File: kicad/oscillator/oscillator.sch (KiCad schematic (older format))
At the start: 19 parts

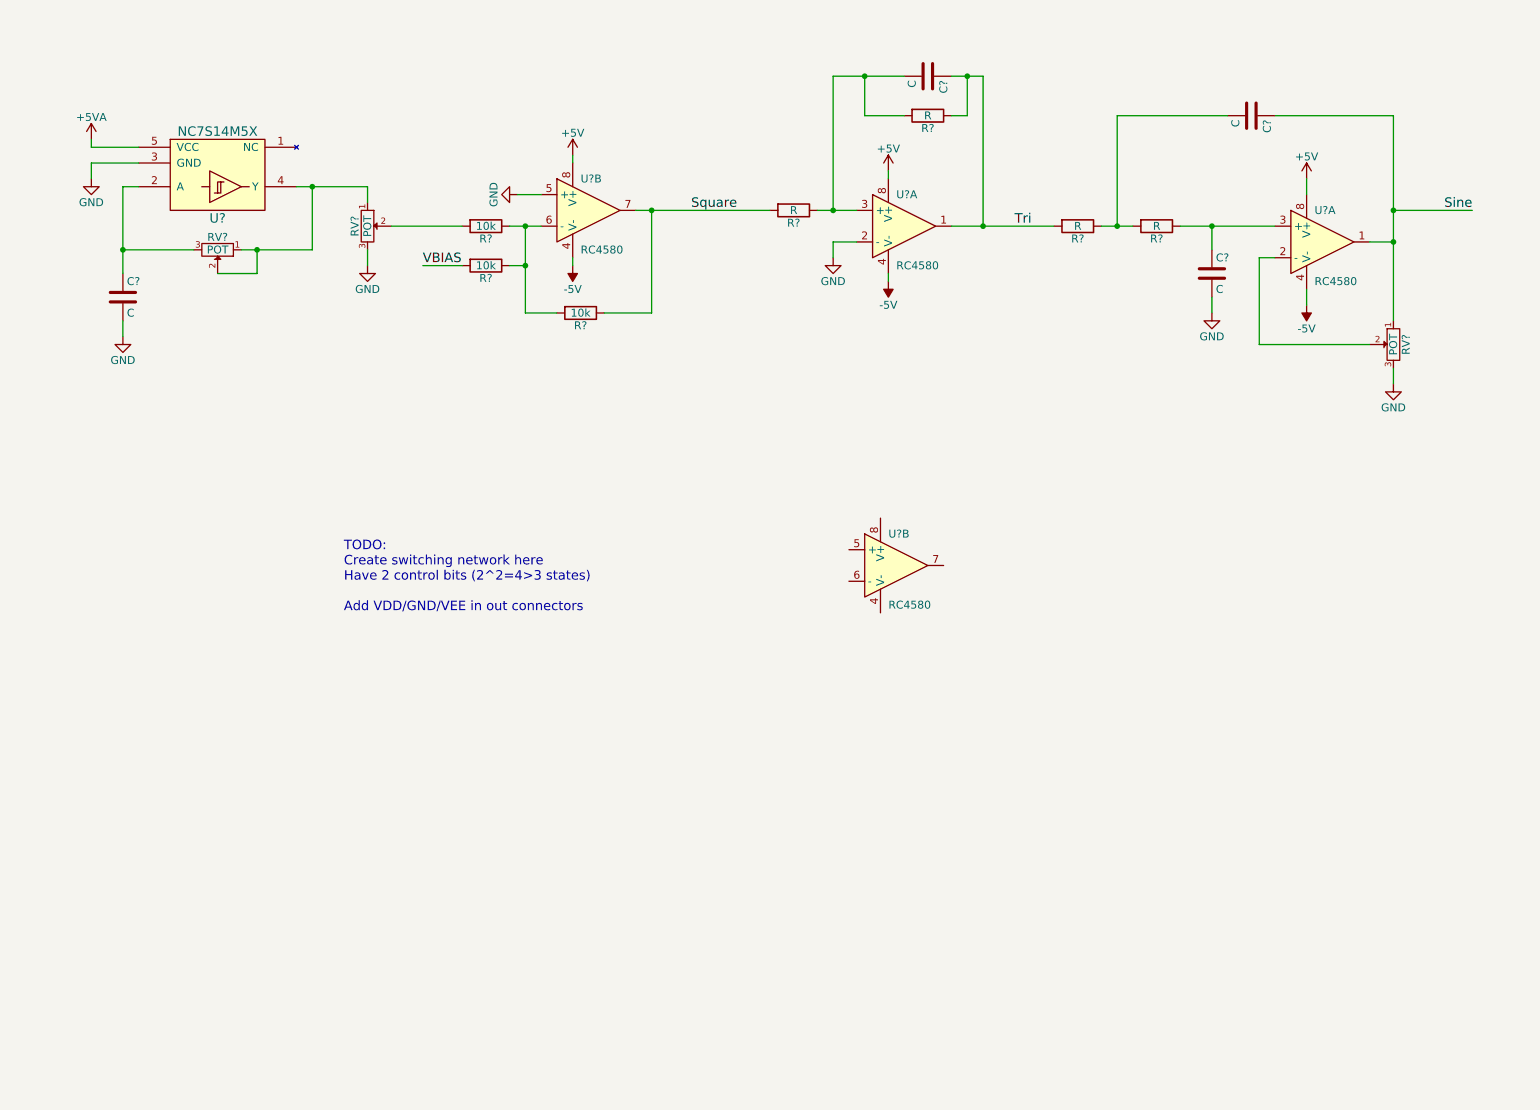
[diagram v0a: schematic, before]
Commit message: [kicad] osc schem done
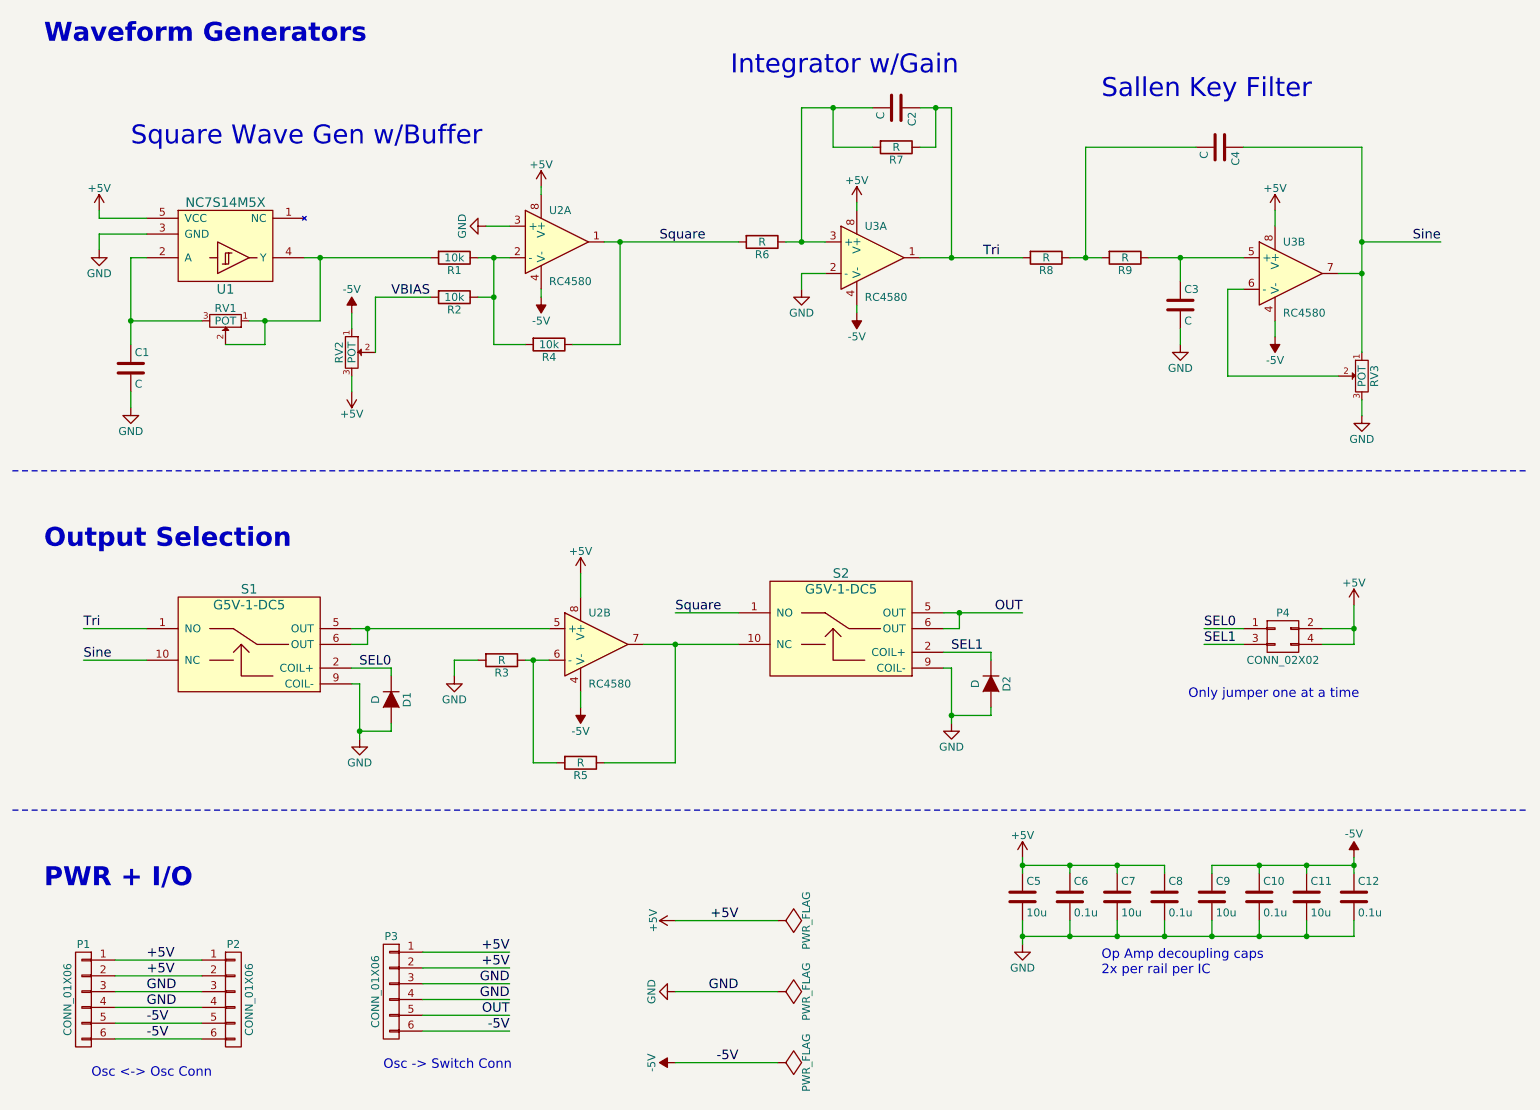
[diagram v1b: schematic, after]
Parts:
- removed RV?: POT, symbol POT
- added C10, C12, C6, C8: 0.1u, Capacitors_SMD:C_0805_HandSoldering, symbol C
- added C11, C5, C7, C9: 10u, Capacitors_SMD:C_0805_HandSoldering, symbol C
- added D1, D2: D, TO_SOT_Packages_SMD:SOT-23, symbol D
- added P1, P2, P3: CONN_01X06, Pin_Headers:Pin_Header_Angled_1x06, symbol CONN_01X06
- added P4: CONN_02X02, Pin_Headers:Pin_Header_Straight_2x02, symbol CONN_02X02
- added R3, R5: R, Resistors_SMD:R_0805_HandSoldering, symbol R
- added RV2: POT, symbol POT
- added S1, S2: G5V-1-DC5, Tone_Matrix:G5V-1, symbol G5V-1-DC5
- C1, C2, C3, C4: renamed from C?; footprint (none) -> Capacitors_SMD:C_0805_HandSoldering
- R1, R2, R4, R6, R7, R8, R9: renamed from R?; footprint (none) -> Resistors_SMD:R_0805_HandSoldering
- U1: renamed from U?; footprint (none) -> TO_SOT_Packages_SMD:SOT-23-5
- U2, U3: renamed from U?; footprint (none) -> Housings_SOIC:SOIC-8_3.9x4.9mm_Pitch1.27mm
- gave numbers to parts that had none: 2
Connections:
- net +5VA is gone; now on net +5V: U1.5 (VCC)
- net +5V: now also U2.8 (V+), C5.1, C6.1, C7.1, C8.1, P1.1 (P1), P1.2 (P2), P2.1 (P1), P2.2 (P2), P3.1 (P1), P3.2 (P2), P4.2 (P2), P4.4 (P4), RV2.3
- net -5V: now also U2.4 (V-), C10.1, C11.1, C12.1, C9.1, P1.5 (P5), P1.6 (P6), P2.5 (P5), P2.6 (P6), P3.6 (P6), RV2.1
- net GND: now also U2.3 (+), C10.2, C11.2, C12.2, C5.2, C6.2, C7.2, C8.2, C9.2, D1.2 (A), D2.2 (A), P1.3 (P3), P1.4 (P4), P2.3 (P3), P2.4 (P4), P3.3 (P3), P3.4 (P4), R3.2, S1.9 (COIL-), S2.9 (COIL-); no longer U2.5 (+)
- net Sine: now also U3.7, S1.10 (NC); no longer U3.1
- net Square: now also U2.1, S2.1 (NO); no longer U2.7
- net Tri: now also S1.1 (NO)
- net VBIAS: now also RV2.2
- net at RV1.1, RV1.2, U1.4 (Y): now also R1.2
- net at R1.1, R2.1, R4.2: now also U2.2 (-); no longer U2.6 (-)
- net at RV3.2: now also U3.6 (-); no longer U3.2 (-)
- net at C3.1, R9.1: now also U3.5 (+); no longer U3.3 (+)
- net at U2.5 (+): now also S1.5 (OUT), S1.6 (OUT)
- net at U2.6 (-): now also R3.1, R5.2
- net at U2.7: now also R5.1, S2.10 (NC)
- new net OUT: P3.5 (P5), S2.5 (OUT), S2.6 (OUT)
- new net SEL0: D1.1 (K), P4.1 (P1), S1.2 (COIL+)
- new net SEL1: D2.1 (K), P4.3 (P3), S2.2 (COIL+)
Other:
- note added: "Integrator w/Gain"
- note added: "Only jumper one at a time"
- note added: "Op Amp decoupling caps\n2x per rail per IC"
- note added: "Osc -> Switch Conn"
- note added: "Osc <-> Osc Conn"
- note added: "Output Selection"
- note added: "PWR + I/O"
- note added: "Sallen Key Filter"
- note added: "Square Wave Gen w/Buffer"
- note added: "Waveform Generators"
- note removed: "TODO:\nCreate switching network here\nHave 2 control bits (2^2=4>3 states)\n\nAdd VDD/GND/VEE in out connectors\n"
- moved on the sheet: C1, C2, C3, C4, R1, R2, R4, R6, R7, R8, R9, RV1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
